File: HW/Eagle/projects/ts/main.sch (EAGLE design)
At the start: 47 parts, among them IC1 4050D, Q1 20 MHz, T1 IRFZ24N, T2 IRFZ24N, U1 ATMEGA328P-PU, U2 LM2576T, U3 HT7533, U4 LM75

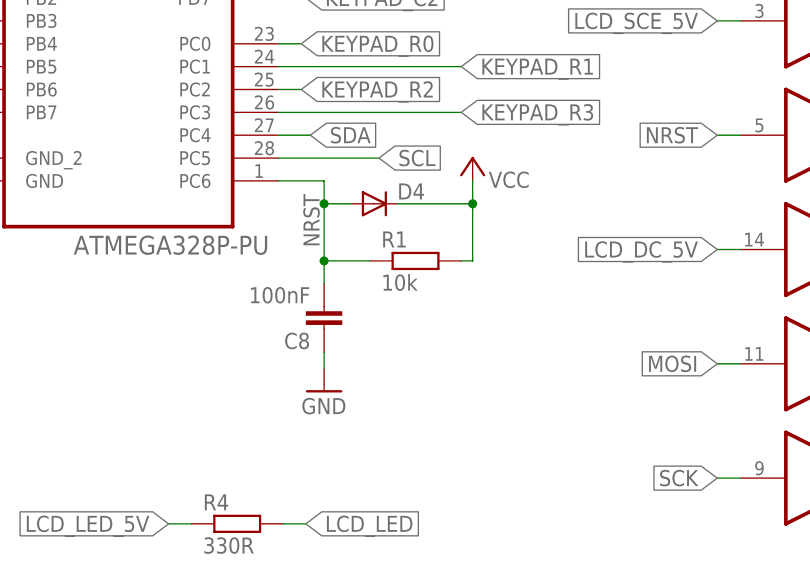
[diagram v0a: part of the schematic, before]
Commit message: Replaced R1 due to improper LCD reset procedure
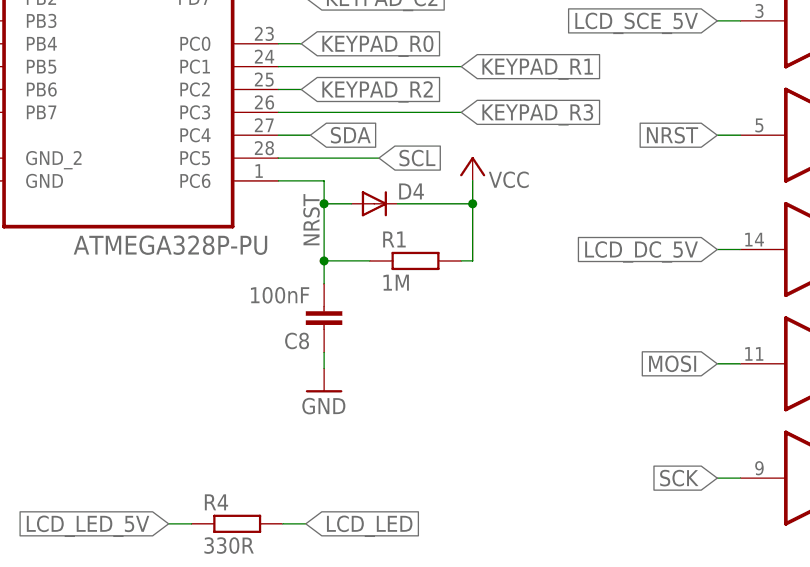
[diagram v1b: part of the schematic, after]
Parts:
- R1: value 10k -> 1M
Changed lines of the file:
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@@
 <part name="C5" library="rcl" deviceset="C-EU" device="C0805" value="15pF"/>
 <part name="P+3" library="supply1" deviceset="VCC" device=""/>
-<part name="R1" library="rcl" deviceset="R-EU_" device="R0805" value="10k"/>
+<part name="R1" library="rcl" deviceset="R-EU_" device="R0805" value="1M"/>
 <part name="R2" library="rcl" deviceset="R-EU_" device="R0805" value="1M"/>
 <part name="ICSP" library="con-lstb" deviceset="MA03-2" device=""/>

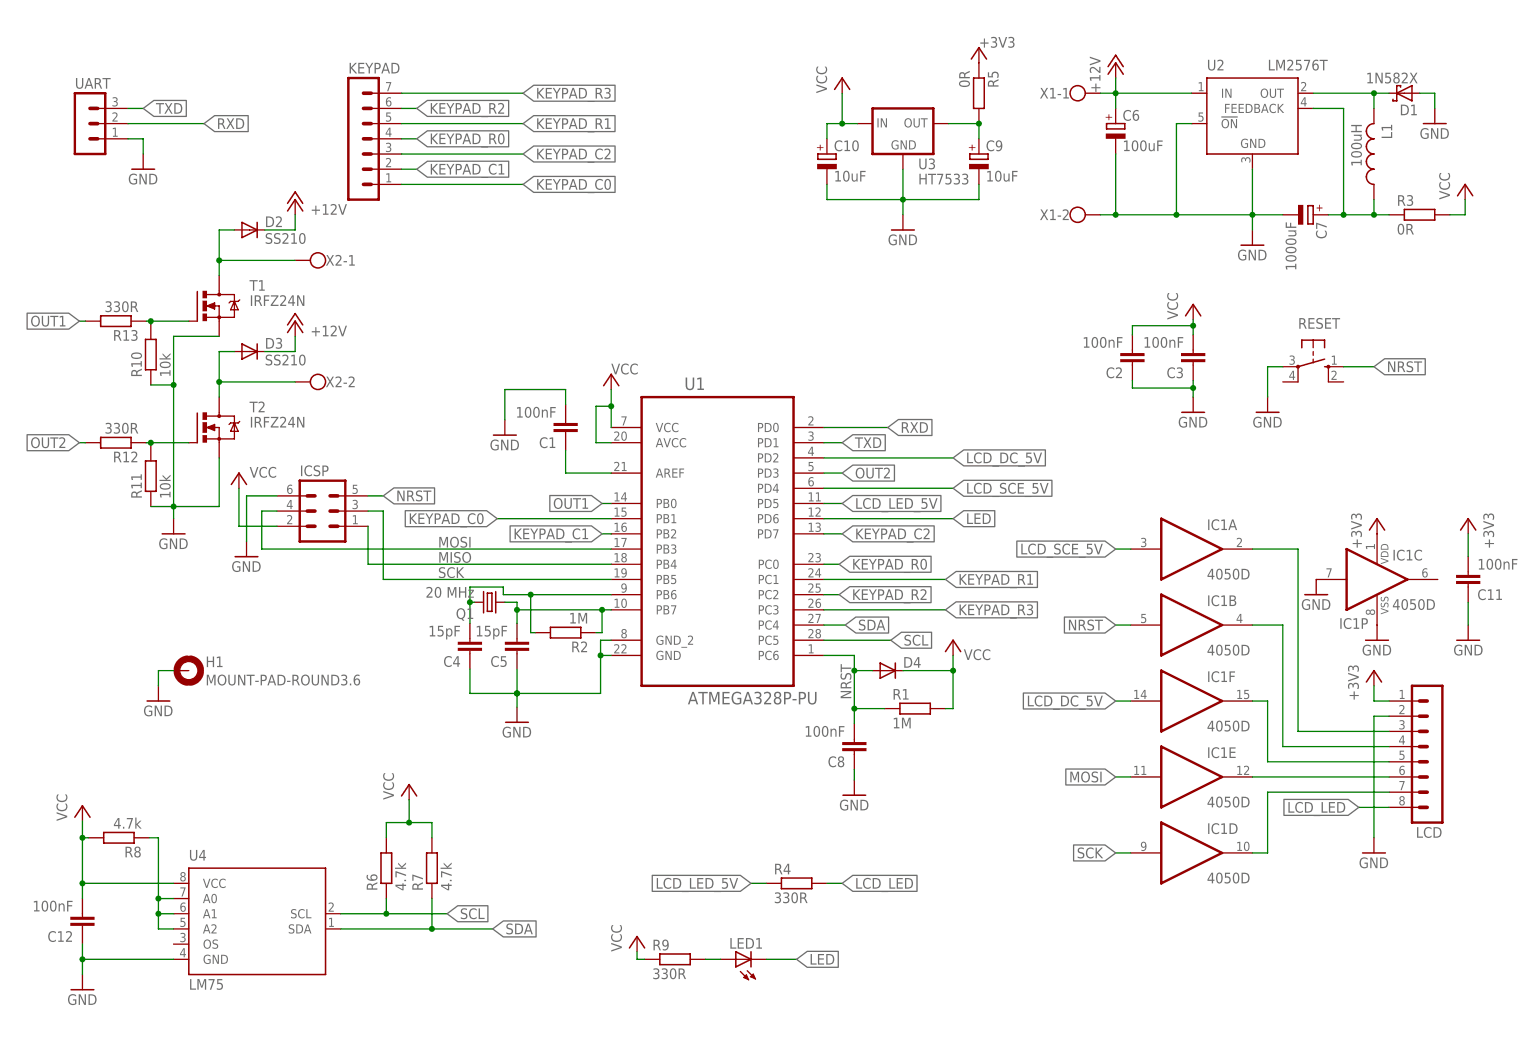
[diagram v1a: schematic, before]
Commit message: [HW] Updated PCB
Fixed keypad connection. Removed copper from underneath the temperature
sensor. Made temperature sensor removable.
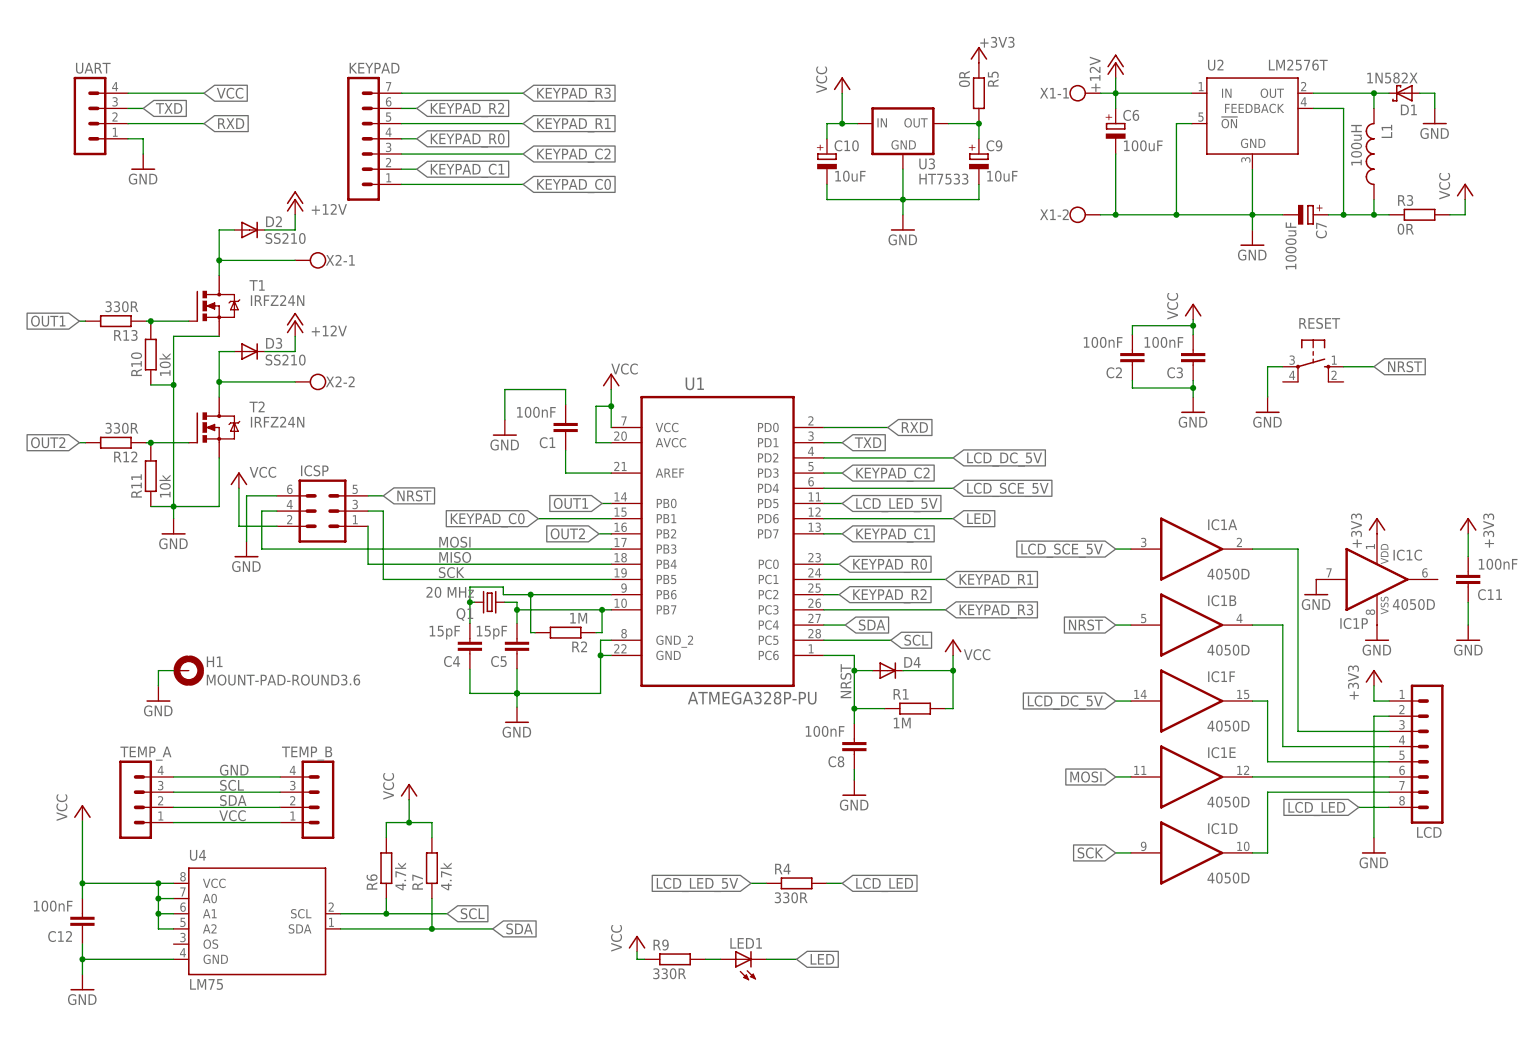
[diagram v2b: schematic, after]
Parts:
- removed R8: 4.7k, rcl:R-EU_R0805
- added TEMP_A, TEMP_B: (no value), con-lstb:MA04-1
- UART: device con-lstb:MA03-1 -> con-lstb:MA04-1
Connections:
- removed net N$5: R8.1, U4.A0, U4.A1, U4.A2
- net GND: now also TEMP_A.4, TEMP_B.4
- net KEYPAD_C1: now also U1.PD7; no longer U1.PB2
- net KEYPAD_C2: now also U1.PD3; no longer U1.PD7
- net OUT2: now also U1.PB2; no longer U1.PD3
- net SCL: now also TEMP_A.3, TEMP_B.3
- net SDA: now also TEMP_A.2, TEMP_B.2
- net VCC: now also TEMP_A.1, TEMP_B.1, U4.A0, U4.A1, U4.A2, UART.4; no longer R8.2

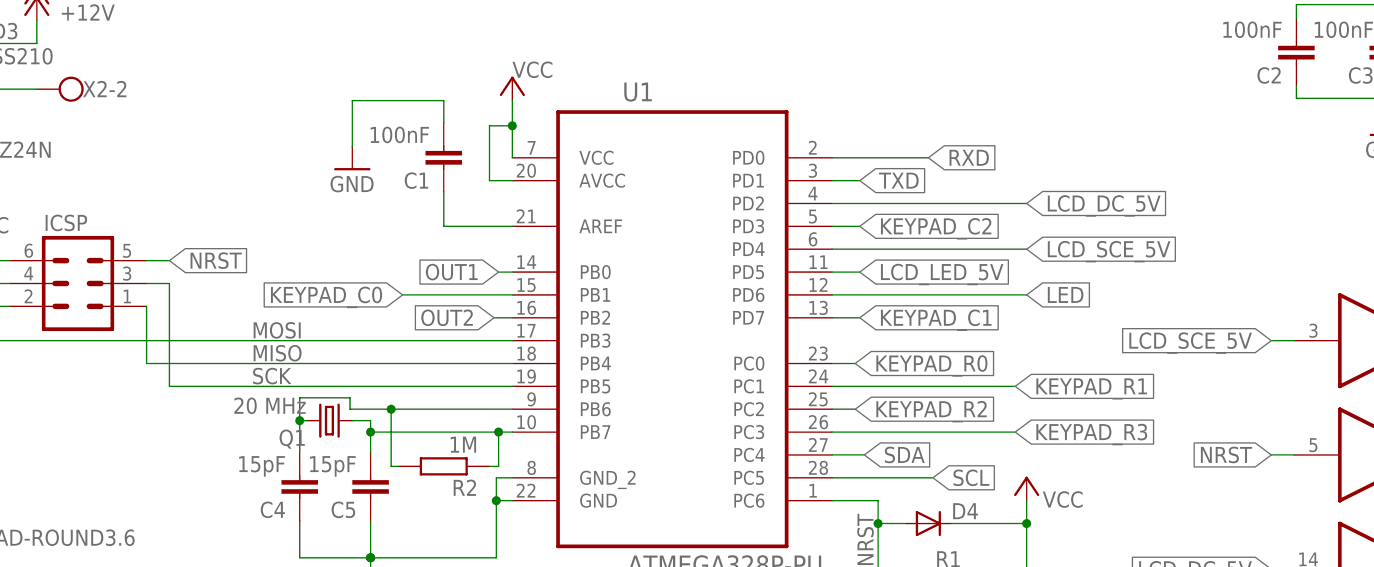
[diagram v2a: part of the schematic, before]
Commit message: [HW] LCD chip select
Using NSS microcontroller output to drive LCD chip select.
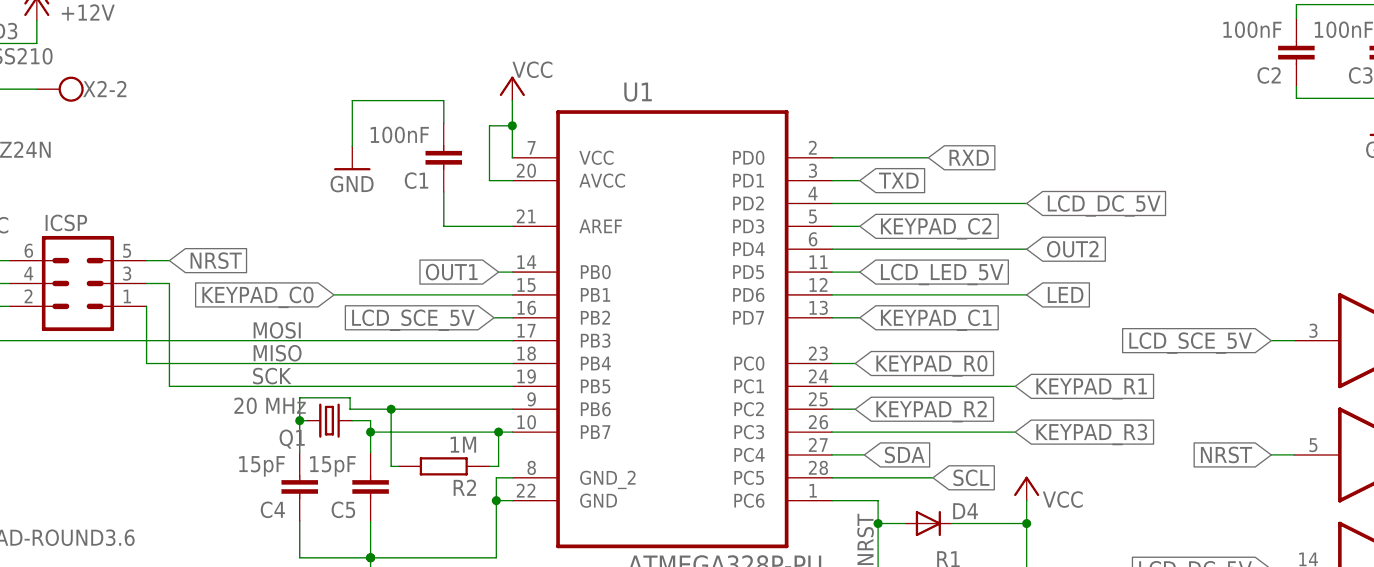
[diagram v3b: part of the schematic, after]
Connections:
- net LCD_SCE_5V: now also U1.PB2; no longer U1.PD4
- net OUT2: now also U1.PD4; no longer U1.PB2
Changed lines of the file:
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@@
 <?xml version="1.0" encoding="utf-8"?>
 <!DOCTYPE eagle SYSTEM "eagle.dtd">
-<eagle version="8.4.3">
+<eagle version="8.5.0">
 <drawing>
 <settings>
@@
 <net name="LCD_SCE_5V" class="0">
 <segment>
-<pinref part="U1" gate="A" pin="PD4"/>
-<wire x1="139.192" y1="93.98" x2="160.782" y2="93.98" width="0.1524" layer="91"/>
-<label x="160.782" y="93.98" size="1.778" layer="95" xref="yes"/>
-</segment>
-<segment>
 <pinref part="IC1" gate="A" pin="I"/>
 <wire x1="190.5" y1="83.82" x2="187.96" y2="83.82" width="0.1524" layer="91"/>
 <label x="187.96" y="83.82" size="1.778" layer="95" rot="R180" xref="yes"/>
+</segment>
+<segment>
+<pinref part="U1" gate="A" pin="PB2"/>
+<wire x1="103.632" y1="86.36" x2="101.6" y2="86.36" width="0.1524" layer="91"/>
+<label x="101.6" y="86.36" size="1.778" layer="95" rot="R180" xref="yes"/>
 </segment>
 </net>
@@
 <segment>
 <pinref part="U1" gate="A" pin="PB1"/>
-<wire x1="103.632" y1="88.9" x2="91.44" y2="88.9" width="0.1524" layer="91"/>
-<label x="91.44" y="88.9" size="1.778" layer="95" rot="R180" xref="yes"/>
+<wire x1="103.632" y1="88.9" x2="83.82" y2="88.9" width="0.1524" layer="91"/>
+<label x="83.82" y="88.9" size="1.778" layer="95" rot="R180" xref="yes"/>
 </segment>
 </net>
@@
 </segment>
 <segment>
-<pinref part="U1" gate="A" pin="PB2"/>
-<wire x1="103.632" y1="86.36" x2="101.6" y2="86.36" width="0.1524" layer="91"/>
-<label x="101.6" y="86.36" size="1.778" layer="95" rot="R180" xref="yes"/>
-</segment>
-</net>
+<pinref part="U1" gate="A" pin="PD4"/>
+<wire x1="139.192" y1="93.98" x2="160.782" y2="93.98" width="0.1524" layer="91"/>
+<label x="160.782" y="93.98" size="1.778" layer="95" xref="yes"/>
+</segment>
+</net>
